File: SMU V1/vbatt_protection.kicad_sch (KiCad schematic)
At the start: 5 parts, among them Q1201 SI2301CDS-T1-GE3

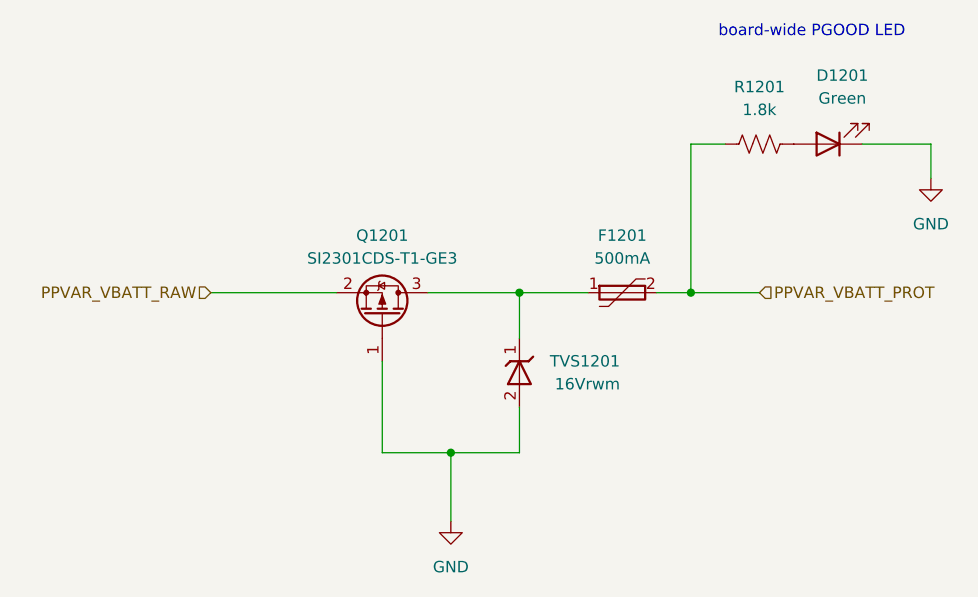
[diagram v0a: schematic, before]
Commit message: halfway done with routing, still needs antenna
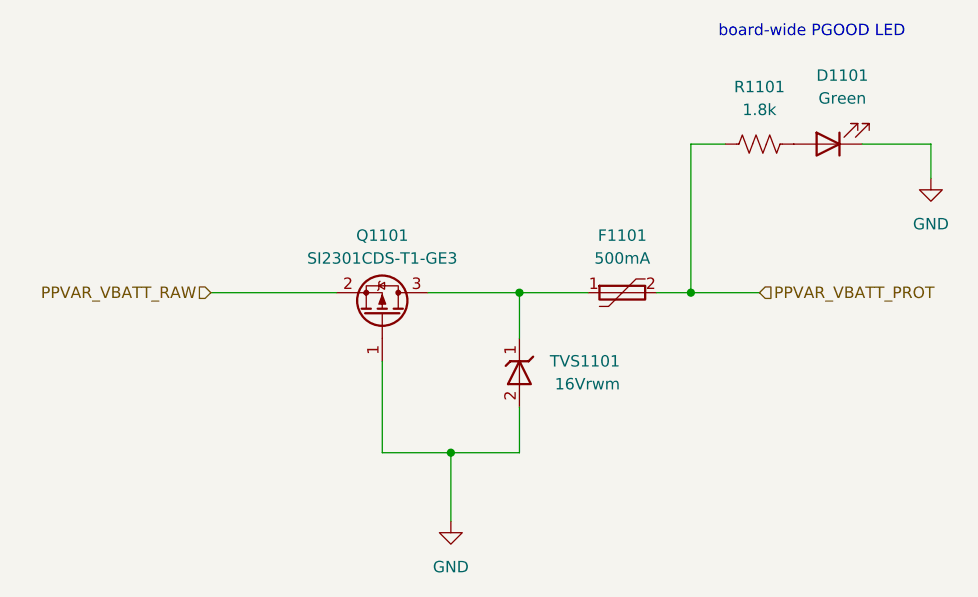
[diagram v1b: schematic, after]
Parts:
- renumbered D1201 to D1101, F1201 to F1101, Q1201 to Q1101, R1201 to R1101, TVS1201 to TVS1101
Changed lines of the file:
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@@
 		(dnp no)
 		(fields_autoplaced yes)
-		(property "Reference" "F1201"
+		(property "Reference" "F1101"
 			(at 152.4 81.28 0)
 			(effects
@@
 			(project ""
 				(path "/1f58b889-96e6-4877-90a3-5a655db5910b/b9f10619-4e5b-45af-b866-c6815d605ed5/ffadd9c2-fe2d-4025-92ac-e8757544fe06"
-					(reference "F1201")
+					(reference "F1101")
 					(unit 1)
 				)
@@
 		(dnp no)
 		(fields_autoplaced yes)
-		(property "Reference" "#PWR01202"
+		(property "Reference" "#PWR01102"
 			(at 186.69 81.28 0)
 			(effects
@@
 			(project "SMU V1"
 				(path "/1f58b889-96e6-4877-90a3-5a655db5910b/b9f10619-4e5b-45af-b866-c6815d605ed5/ffadd9c2-fe2d-4025-92ac-e8757544fe06"
-					(reference "#PWR01202")
+					(reference "#PWR01102")
 					(unit 1)
 				)
@@
 		(on_board yes)
 		(dnp no)
-		(property "Reference" "TVS1201"
+		(property "Reference" "TVS1101"
 			(at 152.146 95.25 90)
 			(effects
@@
 			(project ""
 				(path "/1f58b889-96e6-4877-90a3-5a655db5910b/b9f10619-4e5b-45af-b866-c6815d605ed5/ffadd9c2-fe2d-4025-92ac-e8757544fe06"
-					(reference "TVS1201")
+					(reference "TVS1101")
 					(unit 1)
 				)
@@
 		(dnp no)
 		(fields_autoplaced yes)
-		(property "Reference" "D1201"
+		(property "Reference" "D1101"
 			(at 176.8475 63.5 0)
 			(effects
@@
 			(project ""
 				(path "/1f58b889-96e6-4877-90a3-5a655db5910b/b9f10619-4e5b-45af-b866-c6815d605ed5/ffadd9c2-fe2d-4025-92ac-e8757544fe06"
-					(reference "D1201")
+					(reference "D1101")
 					(unit 1)
 				)
@@
 		(dnp no)
 		(fields_autoplaced yes)
-		(property "Reference" "R1201"
+		(property "Reference" "R1101"
 			(at 167.64 64.77 0)
 			(effects
@@
 			(project ""
 				(path "/1f58b889-96e6-4877-90a3-5a655db5910b/b9f10619-4e5b-45af-b866-c6815d605ed5/ffadd9c2-fe2d-4025-92ac-e8757544fe06"
-					(reference "R1201")
+					(reference "R1101")
 					(unit 1)
 				)
@@
 		(dnp no)
 		(fields_autoplaced yes)
-		(property "Reference" "#PWR01201"
+		(property "Reference" "#PWR01101"
 			(at 133.35 119.38 0)
 			(effects
@@
 			(project ""
 				(path "/1f58b889-96e6-4877-90a3-5a655db5910b/b9f10619-4e5b-45af-b866-c6815d605ed5/ffadd9c2-fe2d-4025-92ac-e8757544fe06"
-					(reference "#PWR01201")
+					(reference "#PWR01101")
 					(unit 1)
 				)
@@
 		(on_board yes)
 		(dnp no)
-		(property "Reference" "Q1201"
+		(property "Reference" "Q1101"
 			(at 125.73 81.28 90)
 			(effects
@@
 			(project ""
 				(path "/1f58b889-96e6-4877-90a3-5a655db5910b/b9f10619-4e5b-45af-b866-c6815d605ed5/ffadd9c2-fe2d-4025-92ac-e8757544fe06"
-					(reference "Q1201")
+					(reference "Q1101")
 					(unit 1)
 				)

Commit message: finished, should prob double check the high frequency stuff
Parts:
- D1101: value Green -> Vbatt PGOOD
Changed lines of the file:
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@@
 			)
 		)
-		(property "Value" "Green"
+		(property "Value" "Vbatt PGOOD"
 			(at 176.8475 66.04 0)
 			(effects
